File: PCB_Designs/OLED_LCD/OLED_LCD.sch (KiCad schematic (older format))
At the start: 27 parts, among them P1 CONN_01X10, P2 CONN_01X16, P3 CONN_01X01, P4 CONN_01X01, P5 CONN_01X01, P6 CONN_01X01, SW1 Rotary_Encoder_Switch, U2 MCP23017, U3 CHERRY-MX

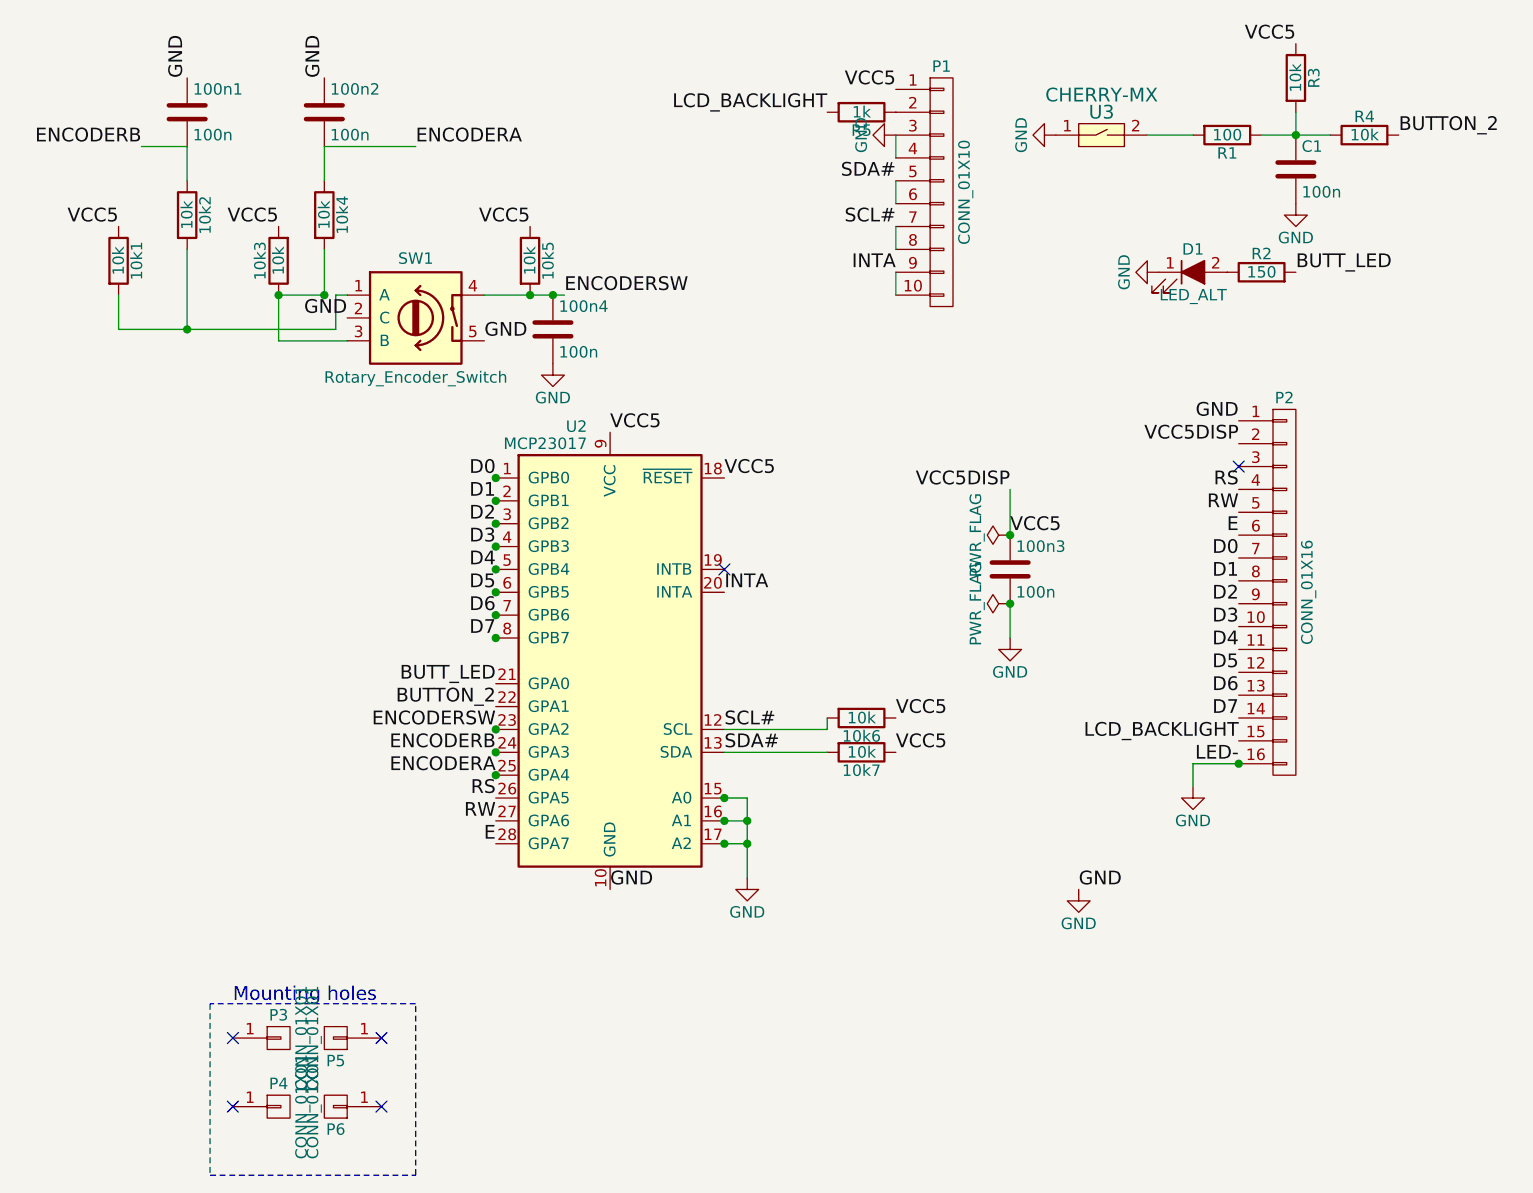
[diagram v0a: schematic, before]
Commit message: LCD board trim pot and transistor
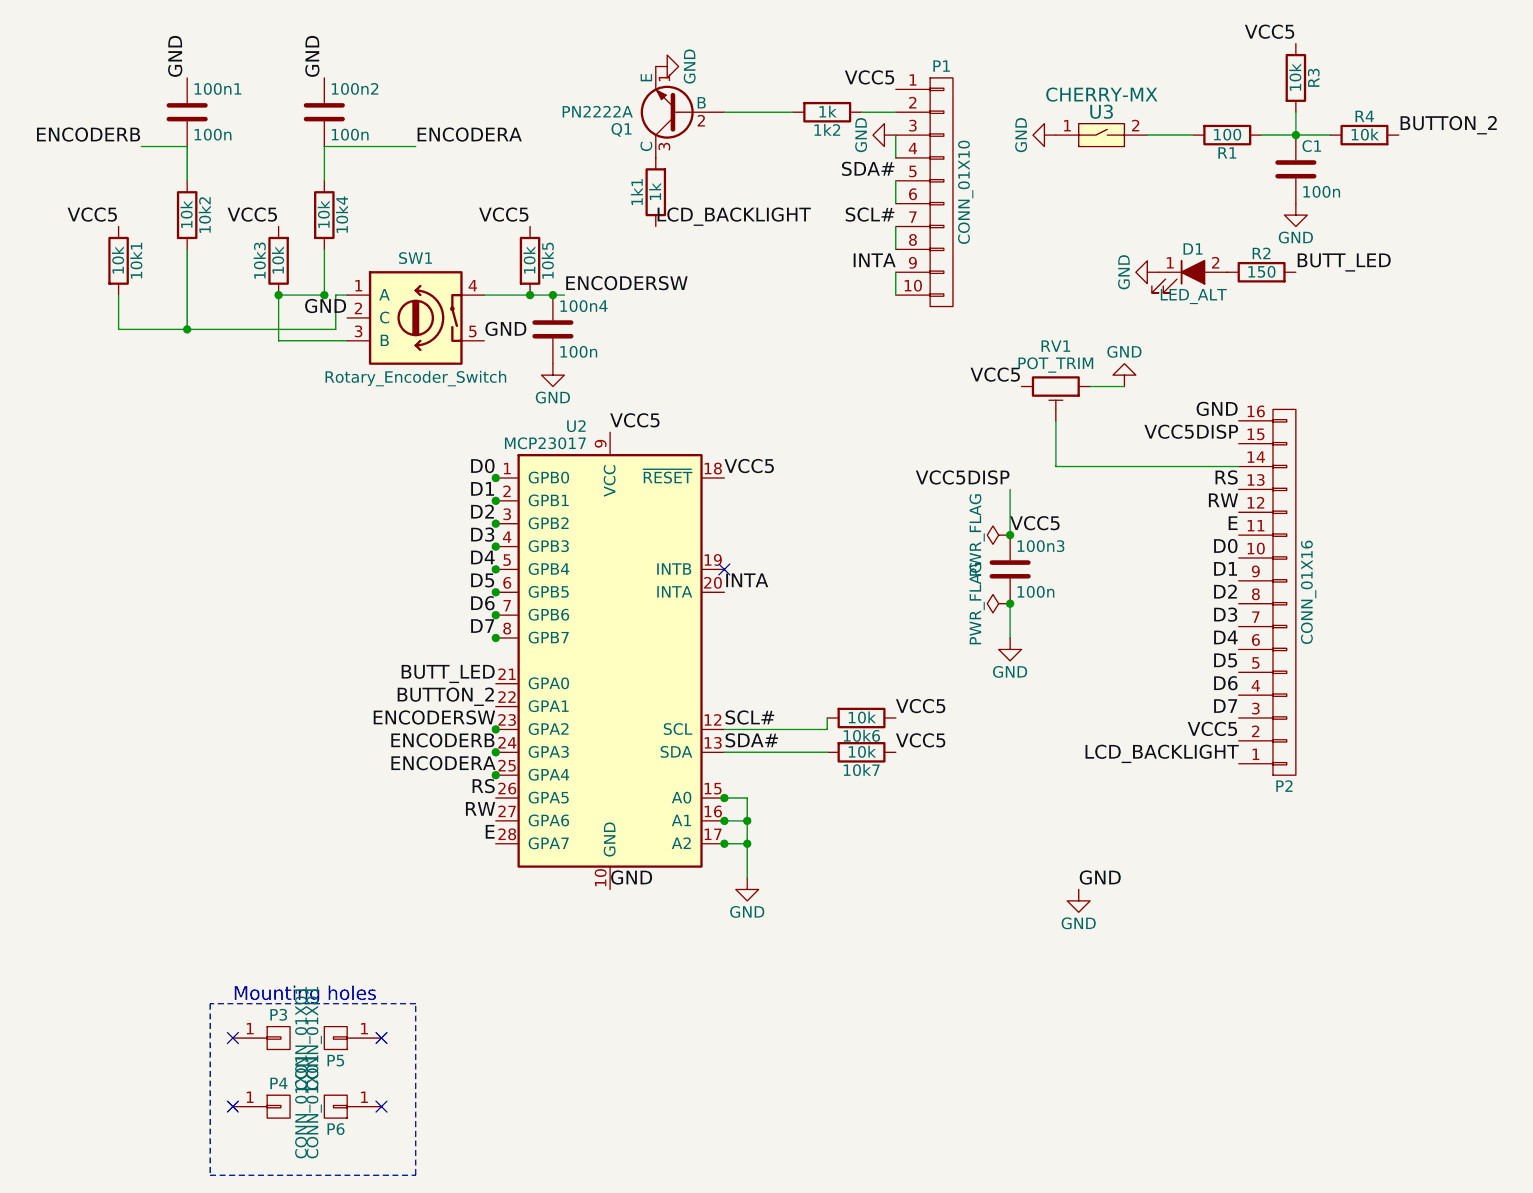
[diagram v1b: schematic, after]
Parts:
- removed R5: 1k, Resistors_SMD:R_0603_HandSoldering, symbol R
- added 1k1, 1k2: 1k, Resistors_SMD:R_0603_HandSoldering, symbol R
- added Q1: PN2222A, TO_SOT_Packages_THT:TO-92_Molded_Narrow, symbol PN2222A
- added RV1: POT_TRIM, symbol POT_TRIM
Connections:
- net D0: now also P2.10 (P10); no longer P2.7 (P7)
- net D1: now also P2.9 (P9); no longer P2.8 (P8)
- net D2: now also P2.8 (P8); no longer P2.9 (P9)
- net D3: now also P2.7 (P7); no longer P2.10 (P10)
- net D4: now also P2.6 (P6); no longer P2.11 (P11)
- net D5: now also P2.5 (P5); no longer P2.12 (P12)
- net D6: now also P2.4 (P4); no longer P2.13 (P13)
- net D7: now also P2.3 (P3); no longer P2.14 (P14)
- net E: now also P2.11 (P11); no longer P2.6 (P6)
- net GND: now also Q1.1 (E), RV1.1; no longer P2.1 (P1)
- net LCD_BACKLIGHT: now also P2.1 (P1), 1k1.1; no longer P2.15 (P15)
- net RS: now also P2.13 (P13); no longer P2.4 (P4)
- net RW: now also P2.12 (P12); no longer P2.5 (P5)
- net VCC5: now also P2.15 (P15), RV1.3
- net at P1.2 (P2): now also 1k2.1
- new net: P2.14 (P14), RV1.2
- new net: 1k2.2, Q1.2 (B)
- new net: 1k1.2, Q1.3 (C)
- no-connect marks 6 -> 5

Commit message: OLED new layout
* Added few components to OLED_LCD pcb.
* Extended PCB layout to make room for all components.
* Generated new LCD photomasks
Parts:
- added 100n5: 100n, Capacitors_SMD:C_0603_HandSoldering, symbol C
- RV1: footprint (none) -> Potentiometers:Potentiometer_Trimmer_ACP_CA9v_Horizontal_Px10.0mm_Py5.0mm
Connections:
- net GND: now also 100n5.2
- net VCC5: now also 100n5.1
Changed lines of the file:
@@
 GND
 $Comp
-L GND #PWR3
+L GND #PWR01
 U 1 1 5894FC28
 P 5150 4300
-F 0 "#PWR3" H 5150 4050 50  0001 C CNN
+F 0 "#PWR01" H 5150 4050 50  0001 C CNN
 F 1 "GND" H 5150 4150 50  0000 C CNN
 F 2 "" H 5150 4300 50  0000 C CNN
@@
 $EndComp
 $Comp
-L GND #PWR5
+L GND #PWR02
 U 1 1 5894FCE6
 P 6300 3250
-F 0 "#PWR5" H 6300 3000 50  0001 C CNN
+F 0 "#PWR02" H 6300 3000 50  0001 C CNN
 F 1 "GND" H 6300 3100 50  0000 C CNN
 F 2 "" H 6300 3250 50  0000 C CNN
@@
 Text Label 7300 2300 2    60   ~ 0
 GND
-Text Label 7300 2400 2    60   ~ 0
-VCC5DISP
 Text Label 7300 2600 2    60   ~ 0
 RS
@@
 D7
 $Comp
-L GND #PWR7
+L GND #PWR03
 U 1 1 589508C9
 P 6600 4350
-F 0 "#PWR7" H 6600 4100 50  0001 C CNN
+F 0 "#PWR03" H 6600 4100 50  0001 C CNN
 F 1 "GND" H 6600 4200 50  0000 C CNN
 F 2 "" H 6600 4350 50  0000 C CNN
@@
 Text Label 5800 1250 2    60   ~ 0
 SDA#
-Text Label 6300 2600 2    60   ~ 0
-VCC5DISP
 $Comp
 L R 10k6
@@
 $EndComp
 $Comp
-L GND #PWR1
+L GND #PWR04
 U 1 1 58A0D2DB
 P 4300 2050
-F 0 "#PWR1" H 4300 1800 50  0001 C CNN
+F 0 "#PWR04" H 4300 1800 50  0001 C CNN
 F 1 "GND" H 4300 1900 50  0000 C CNN
 F 2 "" H 4300 2050 50  0000 C CNN
@@
 BUTTON_2
 $Comp
-L GND #PWR9
+L GND #PWR05
 U 1 1 58A0E8E0
 P 6950 1650
-F 0 "#PWR9" H 6950 1400 50  0001 C CNN
+F 0 "#PWR05" H 6950 1400 50  0001 C CNN
 F 1 "GND" H 6950 1500 50  0000 C CNN
 F 2 "" H 6950 1650 50  0000 C CNN
@@
 $EndComp
 $Comp
-L GND #PWR4
+L GND #PWR06
 U 1 1 58A0F70D
 P 5800 1050
-F 0 "#PWR4" H 5800 800 50  0001 C CNN
+F 0 "#PWR06" H 5800 800 50  0001 C CNN
 F 1 "GND" H 5800 900 50  0000 C CNN
 F 2 "" H 5800 1050 50  0000 C CNN
@@
 VCC5
 $Comp
-L GND #PWR6
+L GND #PWR07
 U 1 1 58A10FD4
 P 6500 1050
-F 0 "#PWR6" H 6500 800 50  0001 C CNN
+F 0 "#PWR07" H 6500 800 50  0001 C CNN
 F 1 "GND" H 6500 900 50  0000 C CNN
 F 2 "" H 6500 1050 50  0000 C CNN
@@
 $EndComp
 $Comp
-L GND #PWR10
+L GND #PWR08
 U 1 1 58A1101A
 P 7550 1350
-F 0 "#PWR10" H 7550 1100 50  0001 C CNN
+F 0 "#PWR08" H 7550 1100 50  0001 C CNN
 F 1 "GND" H 7550 1200 50  0000 C CNN
 F 2 "" H 7550 1350 50  0000 C CNN
@@
 $EndComp
 $Comp
-L PWR_FLAG #FLG1
+L PWR_FLAG #FLG09
 U 1 1 58B2ED0B
 P 6300 2800
-F 0 "#FLG1" H 6300 2875 50  0001 C CNN
+F 0 "#FLG09" H 6300 2875 50  0001 C CNN
 F 1 "PWR_FLAG" H 6300 2950 50  0000 C CNN
 F 2 "" H 6300 2800 50  0001 C CNN
@@
 $EndComp
 $Comp
-L PWR_FLAG #FLG2
+L PWR_FLAG #FLG010
 U 1 1 58B2EF20
 P 6300 3100
-F 0 "#FLG2" H 6300 3175 50  0001 C CNN
+F 0 "#FLG010" H 6300 3175 50  0001 C CNN
 F 1 "PWR_FLAG" H 6300 3250 50  0000 C CNN
 F 2 "" H 6300 3100 50  0001 C CNN
@@
 F 0 "RV1" V 6325 2150 50  0000 C CNN
 F 1 "POT_TRIM" V 6400 2150 50  0000 C CNN
-F 2 "" H 6500 2150 50  0001 C CNN
+F 2 "Potentiometers:Potentiometer_Trimmer_ACP_CA9v_Horizontal_Px10.0mm_Py5.0mm" H 6500 2150 50  0001 C CNN
 F 3 "" H 6500 2150 50  0001 C CNN
 	1    6500 2150
@@
 VCC5
 $Comp
-L GND #PWR8
+L GND #PWR011
 U 1 1 58C6BA3F
 P 6800 2150
-F 0 "#PWR8" H 6800 1900 50  0001 C CNN
+F 0 "#PWR011" H 6800 1900 50  0001 C CNN
 F 1 "GND" H 6800 2000 50  0000 C CNN
 F 2 "" H 6800 2150 50  0000 C CNN
@@
 Connection ~ 4050 3750
 Connection ~ 4050 3850
-Wire Wire Line
-	6300 2600 6300 2800
 Connection ~ 6300 2800
 Wire Wire Line
@@
 	3400 1750 3350 1750
 Wire Wire Line
-	3350 1900 3350 1750
-Wire Wire Line
-	2400 1900 3350 1900
+	3350 1750 3350 1900
+Wire Wire Line
+	3350 1900 2400 1900
 Wire Wire Line
 	6650 2150 6800 2150
@@
 $EndComp
 $Comp
-L GND #PWR2
+L GND #PWR012
 U 1 1 58C6DE1A
 P 4750 750
-F 0 "#PWR2" H 4750 500 50  0001 C CNN
+F 0 "#PWR012" H 4750 500 50  0001 C CNN
 F 1 "GND" H 4750 600 50  0000 C CNN
 F 2 "" H 4750 750 50  0000 C CNN
@@
 Wire Wire Line
 	5050 950  5350 950
+Text Label 7300 2400 2    60   ~ 0
+VCC5
+$Comp
+L C 100n5
+U 1 1 58C72772
+P 6650 2950
+F 0 "100n5" H 6675 3050 50  0000 L CNN
+F 1 "100n" H 6675 2850 50  0000 L CNN
+F 2 "Capacitors_SMD:C_0603_HandSoldering" H 6688 2800 50  0001 C CNN
+F 3 "" H 6650 2950 50  0000 C CNN
+	1    6650 2950
+	1    0    0    -1
+$EndComp
+Wire Wire Line
+	6300 2800 6650 2800
+Wire Wire Line
+	6300 3100 6650 3100
 $EndSCHEMATC

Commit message: Added missing 10k R on OLED board, diodes on Buttons board
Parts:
- added 10k8: 10k, Resistors_SMD:R_0603_HandSoldering, symbol R
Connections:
- net ENCODERSW: now also 10k8.1; no longer 10k5.2, SW1.4
- new net: 10k5.2, 10k8.2, SW1.4
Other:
- moved on the sheet: 100n4
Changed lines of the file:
@@
 	1    0    0    -1
 $EndComp
-Text Label 4350 1750 0    60   ~ 0
+Text Label 4750 1750 0    60   ~ 0
 ENCODERSW
 $Comp
@@
 L C 100n4
 U 1 1 58A0D14F
-P 4300 1900
-F 0 "100n4" H 4325 2000 50  0000 L CNN
-F 1 "100n" H 4325 1800 50  0000 L CNN
-F 2 "Capacitors_SMD:C_0603_HandSoldering" H 4338 1750 50  0001 C CNN
-F 3 "" H 4300 1900 50  0000 C CNN
-	1    4300 1900
+P 4750 1900
+F 0 "100n4" H 4775 2000 50  0000 L CNN
+F 1 "100n" H 4775 1800 50  0000 L CNN
+F 2 "Capacitors_SMD:C_0603_HandSoldering" H 4788 1750 50  0001 C CNN
+F 3 "" H 4750 1900 50  0000 C CNN
+	1    4750 1900
 	1    0    0    -1
 $EndComp
@@
 L GND #PWR04
 U 1 1 58A0D2DB
-P 4300 2050
-F 0 "#PWR04" H 4300 1800 50  0001 C CNN
-F 1 "GND" H 4300 1900 50  0000 C CNN
-F 2 "" H 4300 2050 50  0000 C CNN
-F 3 "" H 4300 2050 50  0000 C CNN
-	1    4300 2050
+P 4750 2050
+F 0 "#PWR04" H 4750 1800 50  0001 C CNN
+F 1 "GND" H 4750 1900 50  0000 C CNN
+F 2 "" H 4750 2050 50  0000 C CNN
+F 3 "" H 4750 2050 50  0000 C CNN
+	1    4750 2050
 	1    0    0    -1
 $EndComp
@@
 Wire Wire Line
 	4000 1750 4350 1750
+Wire Wire Line
+	4650 1750 4750 1750
 Connection ~ 4200 1750
 Wire Wire Line
@@
 Wire Wire Line
 	5050 3750 5500 3750
-Connection ~ 4300 1750
+Connection ~ 4750 1750
 Wire Wire Line
 	6900 1050 7100 1050
@@
 Wire Wire Line
 	6300 3100 6650 3100
+$Comp
+L R 10k8
+U 1 1 58CCB8E2
+P 4500 1750
+F 0 "10k8" V 4580 1750 50  0000 C CNN
+F 1 "10k" V 4500 1750 50  0000 C CNN
+F 2 "Resistors_SMD:R_0603_HandSoldering" V 4430 1750 50  0001 C CNN
+F 3 "" H 4500 1750 50  0000 C CNN
+	1    4500 1750
+	0    1    1    0
+$EndComp
 $EndSCHEMATC
